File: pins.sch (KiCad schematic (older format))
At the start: 12 parts

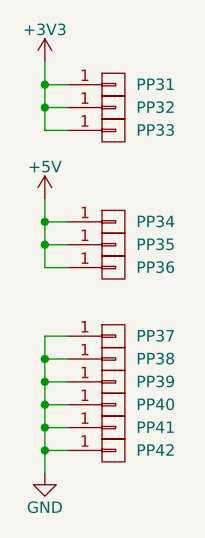
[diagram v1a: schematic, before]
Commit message: Added MCU power control (MCUswitch.sch)
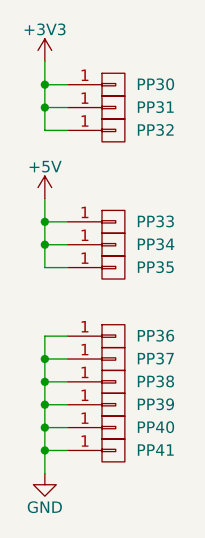
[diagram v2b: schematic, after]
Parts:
- PP41: Supplier (none) -> Farnell
- renumbered PP42 to PP30
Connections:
- net +3V3: now also PP30.1 (P1); no longer PP33.1 (P1)
- net +5V: now also PP33.1 (P1); no longer PP36.1 (P1)
- net GND: now also PP36.1 (P1); no longer PP30.1 (P1)
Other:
- moved on the sheet: PP30, PP31, PP32, PP33, PP34, PP35, PP36, PP37, PP38, PP39, PP40, PP41
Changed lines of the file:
@@
 $Descr A4 11693 8268
 encoding utf-8
-Sheet 4 4
+Sheet 4 5
 Title ""
 Date ""
@@
 L CONN_01X01 PP31
 U 1 1 566CC01D
-P 4450 1600
-F 0 "PP31" H 4550 1600 50  0000 L CNN
-F 1 "CONN_01X01" V 4550 1600 50  0001 C CNN
-F 2 "jakub:PIN_ARRAY_1" H 4450 1600 50  0001 C CNN
-F 3 "" H 4450 1600 50  0000 C CNN
-	1    4450 1600
-	1    0    0    -1
-$EndComp
-$Comp
-L CONN_01X01 PP32
-U 1 1 566CC024
 P 4450 1700
-F 0 "PP32" H 4550 1700 50  0000 L CNN
+F 0 "PP31" H 4550 1700 50  0000 L CNN
 F 1 "CONN_01X01" V 4550 1700 50  0001 C CNN
 F 2 "jakub:PIN_ARRAY_1" H 4450 1700 50  0001 C CNN
@@
 $EndComp
 $Comp
-L CONN_01X01 PP33
-U 1 1 566CC02B
+L CONN_01X01 PP32
+U 1 1 566CC024
 P 4450 1800
-F 0 "PP33" H 4550 1800 50  0000 L CNN
+F 0 "PP32" H 4550 1800 50  0000 L CNN
 F 1 "CONN_01X01" V 4550 1800 50  0001 C CNN
 F 2 "jakub:PIN_ARRAY_1" H 4450 1800 50  0001 C CNN
 F 3 "" H 4450 1800 50  0000 C CNN
 	1    4450 1800
+	1    0    0    -1
+$EndComp
+$Comp
+L CONN_01X01 PP33
+U 1 1 566CC02B
+P 4450 2200
+F 0 "PP33" H 4550 2200 50  0000 L CNN
+F 1 "CONN_01X01" V 4550 2200 50  0001 C CNN
+F 2 "jakub:PIN_ARRAY_1" H 4450 2200 50  0001 C CNN
+F 3 "" H 4450 2200 50  0000 C CNN
+	1    4450 2200
 	1    0    0    -1
 $EndComp
@@
 L CONN_01X01 PP34
 U 1 1 5671D822
-P 4450 2200
-F 0 "PP34" H 4550 2200 50  0000 L CNN
-F 1 "CONN_01X01" V 4550 2200 50  0001 C CNN
-F 2 "jakub:PIN_ARRAY_1" H 4450 2200 50  0001 C CNN
-F 3 "" H 4450 2200 50  0000 C CNN
-	1    4450 2200
-	1    0    0    -1
-$EndComp
-$Comp
-L CONN_01X01 PP35
-U 1 1 5671D828
 P 4450 2300
-F 0 "PP35" H 4550 2300 50  0000 L CNN
+F 0 "PP34" H 4550 2300 50  0000 L CNN
 F 1 "CONN_01X01" V 4550 2300 50  0001 C CNN
 F 2 "jakub:PIN_ARRAY_1" H 4450 2300 50  0001 C CNN
@@
 $EndComp
 $Comp
-L CONN_01X01 PP36
-U 1 1 5671D82E
+L CONN_01X01 PP35
+U 1 1 5671D828
 P 4450 2400
-F 0 "PP36" H 4550 2400 50  0000 L CNN
+F 0 "PP35" H 4550 2400 50  0000 L CNN
 F 1 "CONN_01X01" V 4550 2400 50  0001 C CNN
 F 2 "jakub:PIN_ARRAY_1" H 4450 2400 50  0001 C CNN
@@
 $EndComp
 $Comp
-L CONN_01X01 PP37
-U 1 1 5671D8A0
+L CONN_01X01 PP36
+U 1 1 5671D82E
 P 4450 2700
-F 0 "PP37" H 4550 2700 50  0000 L CNN
+F 0 "PP36" H 4550 2700 50  0000 L CNN
 F 1 "CONN_01X01" V 4550 2700 50  0001 C CNN
 F 2 "jakub:PIN_ARRAY_1" H 4450 2700 50  0001 C CNN
@@
 $EndComp
 $Comp
-L CONN_01X01 PP38
-U 1 1 5671D8A6
+L CONN_01X01 PP37
+U 1 1 5671D8A0
 P 4450 2800
-F 0 "PP38" H 4550 2800 50  0000 L CNN
+F 0 "PP37" H 4550 2800 50  0000 L CNN
 F 1 "CONN_01X01" V 4550 2800 50  0001 C CNN
 F 2 "jakub:PIN_ARRAY_1" H 4450 2800 50  0001 C CNN
@@
 $EndComp
 $Comp
-L CONN_01X01 PP39
-U 1 1 5671D8AC
+L CONN_01X01 PP38
+U 1 1 5671D8A6
 P 4450 2900
-F 0 "PP39" H 4550 2900 50  0000 L CNN
+F 0 "PP38" H 4550 2900 50  0000 L CNN
 F 1 "CONN_01X01" V 4550 2900 50  0001 C CNN
 F 2 "jakub:PIN_ARRAY_1" H 4450 2900 50  0001 C CNN
@@
 $EndComp
 $Comp
-L CONN_01X01 PP40
-U 1 1 5671D918
+L CONN_01X01 PP39
+U 1 1 5671D8AC
 P 4450 3000
-F 0 "PP40" H 4550 3000 50  0000 L CNN
+F 0 "PP39" H 4550 3000 50  0000 L CNN
 F 1 "CONN_01X01" V 4550 3000 50  0001 C CNN
 F 2 "jakub:PIN_ARRAY_1" H 4450 3000 50  0001 C CNN
@@
 $EndComp
 $Comp
-L CONN_01X01 PP41
-U 1 1 5671D91E
+L CONN_01X01 PP40
+U 1 1 5671D918
 P 4450 3100
-F 0 "PP41" H 4550 3100 50  0000 L CNN
+F 0 "PP40" H 4550 3100 50  0000 L CNN
 F 1 "CONN_01X01" V 4550 3100 50  0001 C CNN
 F 2 "jakub:PIN_ARRAY_1" H 4450 3100 50  0001 C CNN
@@
 $EndComp
 $Comp
-L CONN_01X01 PP42
-U 1 1 5671D924
+L CONN_01X01 PP41
+U 1 1 5671D91E
 P 4450 3200
-F 0 "PP42" H 4550 3200 50  0000 L CNN
+F 0 "PP41" H 4550 3200 50  0000 L CNN
 F 1 "CONN_01X01" V 4550 3200 50  0001 C CNN
 F 2 "jakub:PIN_ARRAY_1" H 4450 3200 50  0001 C CNN
 F 3 "" H 4450 3200 50  0000 C CNN
+F 4 "Farnell" H 4450 3200 60  0001 C CNN "Supplier"
 	1    4450 3200
 	1    0    0    -1
 $EndComp
+$Comp
+L CONN_01X01 PP30
+U 1 1 5671D924
+P 4450 1600
+F 0 "PP30" H 4550 1600 50  0000 L CNN
+F 1 "CONN_01X01" V 4550 1600 50  0001 C CNN
+F 2 "jakub:PIN_ARRAY_1" H 4450 1600 50  0001 C CNN
+F 3 "" H 4450 1600 50  0000 C CNN
+	1    4450 1600
+	1    0    0    -1
+$EndComp

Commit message: Finished adding full part descriptions
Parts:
- PP41: Supplier Farnell -> (none)
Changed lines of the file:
@@
 F 2 "jakub:PIN_ARRAY_1" H 4450 3200 50  0001 C CNN
 F 3 "" H 4450 3200 50  0000 C CNN
-F 4 "Farnell" H 4450 3200 60  0001 C CNN "Supplier"
 	1    4450 3200
 	1    0    0    -1

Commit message: Incorporated un-pulled changes
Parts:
- added P10, P11, P12, P8, P9: 1x8 header strip, symbol CONN_01X08
- added P13: 1x10 header strip, symbol CONN_01X10
- added P14: 2x3 socket strip, symbol CONN_02X03
- added P7: 2x18 header strip, symbol CONN_02X18
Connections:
- no-connect marks 0 -> 92
